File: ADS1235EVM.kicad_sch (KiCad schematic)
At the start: 60 parts, among them J1 Conn_01x04_Pin, J2 Conn_01x11_Pin, U1 ADS1235QWRHMRQ1, U2 LM27762, U5 UCC27524DGN

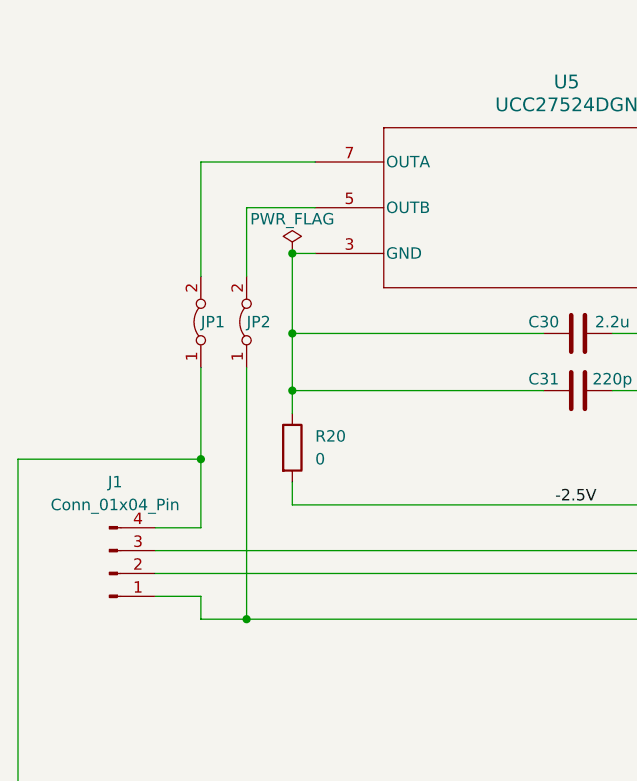
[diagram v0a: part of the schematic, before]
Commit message: Schematic - Jumpers removed + ERC OK
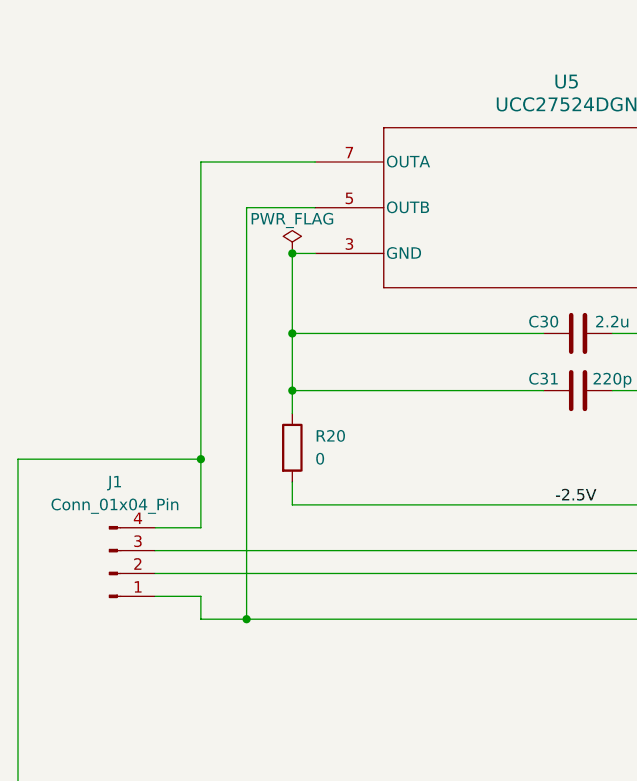
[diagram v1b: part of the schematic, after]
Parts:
- removed JP1, JP2: Jumper_2_Bridged, Jumper:SolderJumper-2_P1.3mm_Open_RoundedPad1.0x1.5mm, symbol Jumper:Jumper_2_Bridged
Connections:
- net at U5.5 (OUTB): now also J1.1 (Pin_1), R16.1
- net at U5.7 (OUTA): now also J1.4 (Pin_4), R17.1
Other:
- company: (none) -> LAAS - CNRS
- title: (none) -> Analog conditioning and filtering measurements
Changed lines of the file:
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@@
 (kicad_sch (version 20230121) (generator eeschema)
   (paper "A4")
+  (title_block
+    (title "Analog conditioning and filtering measurements")
+    (company "LAAS - CNRS")
+  )
   (junction (at 57.15 21.59) (diameter 0) (color 0 0 0 0)
   )
@@
     (stroke (width 0) (type default))
   )
-  (wire (pts (xy 41.91 114.3) (xy 41.91 142.24))
+  (wire (pts (xy 41.91 96.52) (xy 41.91 142.24))
     (stroke (width 0) (type default))
   )
@@
     (stroke (width 0) (type default))
   )
-  (wire (pts (xy 36.83 114.3) (xy 36.83 124.46))
+  (wire (pts (xy 36.83 91.44) (xy 36.83 124.46))
     (stroke (width 0) (type default))
   )
@@
     (stroke (width 0) (type default))
   )
-  (wire (pts (xy 41.91 96.52) (xy 41.91 104.14))
-    (stroke (width 0) (type default))
-  )
   (wire (pts (xy 109.22 59.69) (xy 109.22 63.5))
     (stroke (width 0) (type default))
@@
     (stroke (width 0) (type default))
   )
-  (wire (pts (xy 36.83 91.44) (xy 36.83 104.14))
-    (stroke (width 0) (type default))
-  )
   (wire (pts (xy 166.37 133.35) (xy 166.37 113.03))
     (stroke (width 0) (type default))
@@
     )
   )
-  (symbol (lib_id "Jumper:Jumper_2_Bridged") (at 41.91 109.22 90) (unit 1)
-    (in_bom yes) (on_board yes) (dnp no)
-    (property "Reference" "JP2" (at 41.91 109.22 90)
-      (effects (font (size 1.27 1.27)) (justify right))
-    )
-    (property "Value" "Jumper_2_Bridged" (at 22.86 107.95 90)
-      (effects (font (size 1.27 1.27)) (justify right) hide)
-    )
-    (property "Footprint" "Jumper:SolderJumper-2_P1.3mm_Open_RoundedPad1.0x1.5mm" (at 41.91 109.22 0)
-      (effects (font (size 1.27 1.27)) hide)
-    )
-    (property "Datasheet" "~" (at 41.91 109.22 0)
-      (effects (font (size 1.27 1.27)) hide)
-    )
-    (pin "1")
-    (pin "2")
-    (instances
-      (project "ADS1235EVM"
-        (path "/4faaba4a-da34-4767-a6c4-a9ccb9f4f95a"
-          (reference "JP2") (unit 1)
-        )
-      )
-      (project "PrincipleSchematicV4"
-        (path "/eda615d8-e9fe-47dd-8aa4-13a32693ef53"
-          (reference "JP2") (unit 1)
-        )
-      )
-    )
-  )
   (symbol (lib_id "Device:C") (at 236.22 134.62 0) (unit 1)
     (in_bom yes) (on_board yes) (dnp no)
@@
         )
       )
-    )
-  )
-  (symbol (lib_id "Jumper:Jumper_2_Bridged") (at 36.83 109.22 90) (unit 1)
-    (in_bom yes) (on_board yes) (dnp no)
-    (property "Reference" "JP1" (at 36.83 109.22 90)
-      (effects (font (size 1.27 1.27)) (justify right))
-    )
-    (property "Value" "Jumper_2_Bridged" (at 17.78 107.95 90)
-      (effects (font (size 1.27 1.27)) (justify right) hide)
-    )
-    (property "Footprint" "Jumper:SolderJumper-2_P1.3mm_Open_RoundedPad1.0x1.5mm" (at 36.83 109.22 0)
-      (effects (font (size 1.27 1.27)) hide)
-    )
-    (property "Datasheet" "~" (at 36.83 109.22 0)
-      (effects (font (size 1.27 1.27)) hide)
-    )
-    (pin "1")
-    (pin "2")
-    (instances
-      (project "ADS1235EVM"
-        (path "/4faaba4a-da34-4767-a6c4-a9ccb9f4f95a"
-          (reference "JP1") (unit 1)
-        )
-      )
-      (project "PrincipleSchematicV4"
-        (path "/eda615d8-e9fe-47dd-8aa4-13a32693ef53"
-          (reference "JP1") (unit 1)
-        )
-      )

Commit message: Schematic - Add of 2 jumpers to handle AC & DC excitation
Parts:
- added JP1: Jumper_2_Bridged, symbol Jumper:Jumper_2_Bridged
- added JP2: Jumper_2_Open, symbol Jumper:Jumper_2_Open
- added R22: 100k, Resistor_SMD:R_0402_1005Metric, symbol Device:R
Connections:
- net Avdd is gone; now on net -2.5V: C20.1, C22.1, C23.1, R21.1, R29.2, U1.4 (AVDD)
- net at R33.2, U5.2 (INA): now also JP1.1 (A), JP2.2 (B); no longer R35.2
- net at C30.2, C31.2, R21.2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: now also R22.2
- new net: JP2.1 (A), R35.2
- new net: JP1.2 (B), R22.1
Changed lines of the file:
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@@
   (junction (at 46.99 116.84) (diameter 0) (color 0 0 0 0)
   )
-  (junction (at 115.57 90.17) (diameter 0) (color 0 0 0 0)
-  )
   (junction (at 113.03 129.54) (diameter 0) (color 0 0 0 0)
   )
@@
   (junction (at 109.22 38.1) (diameter 0) (color 0 0 0 0)
   )
+  (junction (at 116.84 77.47) (diameter 0) (color 0 0 0 0)
+  )
   (junction (at 109.22 63.5) (diameter 0) (color 0 0 0 0)
   )
@@
   (junction (at 143.51 177.8) (diameter 0) (color 0 0 0 0)
   )
+  (junction (at 120.65 63.5) (diameter 0) (color 0 0 0 0)
+  )
   (junction (at 64.77 36.83) (diameter 0) (color 0 0 0 0)
   )
+  (junction (at 109.22 77.47) (diameter 0) (color 0 0 0 0)
+  )
   (junction (at 143.51 167.64) (diameter 0) (color 0 0 0 0)
   )
@@
     (stroke (width 0) (type default))
   )
-  (wire (pts (xy 109.22 63.5) (xy 170.18 63.5))
+  (wire (pts (xy 109.22 63.5) (xy 120.65 63.5))
     (stroke (width 0) (type default))
   )
@@
     (stroke (width 0) (type default))
   )
+  (wire (pts (xy 120.65 63.5) (xy 120.65 60.96))
+    (stroke (width 0) (type default))
+  )
   (wire (pts (xy 106.68 49.53) (xy 106.68 53.34))
     (stroke (width 0) (type default))
@@
     (stroke (width 0) (type default))
   )
+  (wire (pts (xy 116.84 115.57) (xy 116.84 119.38))
+    (stroke (width 0) (type default))
+  )
   (wire (pts (xy 148.59 187.96) (xy 148.59 186.69))
     (stroke (width 0) (type default))
@@
     (stroke (width 0) (type default))
   )
+  (wire (pts (xy 116.84 77.47) (xy 116.84 78.74))
+    (stroke (width 0) (type default))
+  )
   (wire (pts (xy 238.76 54.61) (xy 271.78 54.61))
     (stroke (width 0) (type default))
@@
     (stroke (width 0) (type default))
   )
-  (wire (pts (xy 120.65 67.31) (xy 120.65 60.96))
-    (stroke (width 0) (type default))
-  )
   (wire (pts (xy 240.03 116.84) (xy 240.03 119.38))
     (stroke (width 0) (type default))
@@
     (stroke (width 0) (type default))
   )
-  (wire (pts (xy 115.57 90.17) (xy 120.65 90.17))
-    (stroke (width 0) (type default))
-  )
   (wire (pts (xy 139.7 133.35) (xy 143.51 133.35))
     (stroke (width 0) (type default))
@@
     (stroke (width 0) (type default))
   )
-  (wire (pts (xy 106.68 49.53) (xy 109.22 49.53))
+  (wire (pts (xy 109.22 77.47) (xy 109.22 90.17))
     (stroke (width 0) (type default))
   )
-  (wire (pts (xy 109.22 90.17) (xy 115.57 90.17))
+  (wire (pts (xy 106.68 49.53) (xy 109.22 49.53))
     (stroke (width 0) (type default))
   )
@@
     (stroke (width 0) (type default))
   )
+  (wire (pts (xy 120.65 63.5) (xy 170.18 63.5))
+    (stroke (width 0) (type default))
+  )
   (wire (pts (xy 236.22 88.9) (xy 241.3 88.9))
     (stroke (width 0) (type default))
@@
     (stroke (width 0) (type default))
   )
+  (wire (pts (xy 116.84 77.47) (xy 120.65 77.47))
+    (stroke (width 0) (type default))
+  )
   (wire (pts (xy 143.51 167.64) (xy 148.59 167.64))
     (stroke (width 0) (type default))
@@
     (stroke (width 0) (type default))
   )
+  (wire (pts (xy 116.84 86.36) (xy 116.84 87.63))
+    (stroke (width 0) (type default))
+  )
   (wire (pts (xy 170.18 121.92) (xy 170.18 167.64))
     (stroke (width 0) (type default))
@@
     (stroke (width 0) (type default))
   )
+  (wire (pts (xy 120.65 67.31) (xy 120.65 63.5))
+    (stroke (width 0) (type default))
+  )
   (wire (pts (xy 119.38 49.53) (xy 119.38 50.8))
     (stroke (width 0) (type default))
@@
     (stroke (width 0) (type default))
   )
-  (wire (pts (xy 115.57 87.63) (xy 115.57 90.17))
+  (wire (pts (xy 109.22 76.2) (xy 109.22 77.47))
     (stroke (width 0) (type default))
   )
@@
     (stroke (width 0) (type default))
   )
+  (wire (pts (xy 109.22 77.47) (xy 116.84 77.47))
+    (stroke (width 0) (type default))
+  )
   (wire (pts (xy 236.22 91.44) (xy 241.3 91.44))
     (stroke (width 0) (type default))
@@
     (stroke (width 0) (type default))
   )
-  (wire (pts (xy 120.65 90.17) (xy 120.65 74.93))
+  (wire (pts (xy 120.65 77.47) (xy 120.65 74.93))
     (stroke (width 0) (type default))
   )
@@
     (stroke (width 0) (type default))
   )
-  (wire (pts (xy 116.84 97.79) (xy 116.84 119.38))
+  (wire (pts (xy 116.84 97.79) (xy 116.84 105.41))
     (stroke (width 0) (type default))
   )
@@
     )
   )
+  (symbol (lib_id "Jumper:Jumper_2_Open") (at 116.84 110.49 90) (unit 1)
+    (in_bom yes) (on_board yes) (dnp no) (fields_autoplaced)
+    (property "Reference" "JP2" (at 118.11 109.22 90)
+      (effects (font (size 1.27 1.27)) (justify right))
+    )
+    (property "Value" "Jumper_2_Open" (at 118.11 111.76 90)
+      (effects (font (size 1.27 1.27)) (justify right))
+    )
+    (property "Footprint" "" (at 116.84 110.49 0)
+      (effects (font (size 1.27 1.27)) hide)
+    )
+    (property "Datasheet" "~" (at 116.84 110.49 0)
+      (effects (font (size 1.27 1.27)) hide)
+    )
+    (pin "1")
+    (pin "2")
+    (instances
+      (project "ADS1235EVM"
+        (path "/4faaba4a-da34-4767-a6c4-a9ccb9f4f95a"
+          (reference "JP2") (unit 1)
+        )
+      )
+    )
+  )
   (symbol (lib_id "Device:R") (at 231.14 59.69 90) (unit 1)
     (in_bom yes) (on_board yes) (dnp no)
@@
   (symbol (lib_id "Device:R") (at 113.03 123.19 180) (unit 1)
     (in_bom yes) (on_board yes) (dnp no)
-    (property "Reference" "R36" (at 107.95 121.92 0)
-      (effects (font (size 1.27 1.27)) (justify right) hide)
+    (property "Reference" "R36" (at 110.49 124.46 90)
+      (effects (font (size 1.27 1.27)) (justify right))
     )
     (property "Value" "100k" (at 113.03 125.73 90)
@@
     )
   )
-  (symbol (lib_id "power:PWR_FLAG") (at 115.57 87.63 0) (unit 1)
+  (symbol (lib_id "power:PWR_FLAG") (at 109.22 76.2 0) (unit 1)
     (in_bom yes) (on_board yes) (dnp no)
-    (property "Reference" "#FLG04" (at 115.57 85.725 0)
+    (property "Reference" "#FLG04" (at 109.22 74.295 0)
       (effects (font (size 1.27 1.27)) hide)
     )
-    (property "Value" "PWR_FLAG" (at 115.57 83.82 0)
+    (property "Value" "PWR_FLAG" (at 109.22 72.39 0)
       (effects (font (size 1.27 1.27)))
     )
-    (property "Footprint" "" (at 115.57 87.63 0)
+    (property "Footprint" "" (at 109.22 76.2 0)
       (effects (font (size 1.27 1.27)) hide)
     )
-    (property "Datasheet" "~" (at 115.57 87.63 0)
+    (property "Datasheet" "~" (at 109.22 76.2 0)
       (effects (font (size 1.27 1.27)) hide)
     )
@@
     )
   )
+  (symbol (lib_id "Jumper:Jumper_2_Bridged") (at 116.84 92.71 90) (unit 1)
+    (in_bom yes) (on_board yes) (dnp no) (fields_autoplaced)
+    (property "Reference" "JP1" (at 118.11 91.44 90)
+      (effects (font (size 1.27 1.27)) (justify right))
+    )
+    (property "Value" "Jumper_2_Bridged" (at 118.11 93.98 90)
+      (effects (font (size 1.27 1.27)) (justify right))
+    )
+    (property "Footprint" "" (at 116.84 92.71 0)
+      (effects (font (size 1.27 1.27)) hide)
+    )
+    (property "Datasheet" "~" (at 116.84 92.71 0)
+      (effects (font (size 1.27 1.27)) hide)
+    )
+    (pin "1")
+    (pin "2")
+    (instances
+      (project "ADS1235EVM"
+        (path "/4faaba4a-da34-4767-a6c4-a9ccb9f4f95a"
+          (reference "JP1") (unit 1)
+        )
+      )
+    )
+  )
   (symbol (lib_id "power:GND") (at 81.28 63.5 0) (unit 1)
     (in_bom yes) (on_board yes) (dnp no)
@@
     )
   )
+  (symbol (lib_id "Device:R") (at 116.84 82.55 180) (unit 1)
+    (in_bom yes) (on_board yes) (dnp no)
+    (property "Reference" "R22" (at 119.38 83.82 90)
+      (effects (font (size 1.27 1.27)) (justify right))
+    )
+    (property "Value" "100k" (at 116.84 85.09 90)
+      (effects (font (size 1.27 1.27)) (justify right))
+    )
+    (property "Footprint" "Resistor_SMD:R_0402_1005Metric" (at 118.618 82.55 90)
+      (effects (font (size 1.27 1.27)) hide)
+    )
+    (property "Datasheet" "~" (at 116.84 82.55 0)
+      (effects (font (size 1.27 1.27)) hide)
+    )
+    (pin "1")
+    (pin "2")
+    (instances
+      (project "ADS1235EVM"
+        (path "/4faaba4a-da34-4767-a6c4-a9ccb9f4f95a"
+          (reference "R22") (unit 1)
+        )
+      )
+      (project "PrincipleSchematicV4"
+        (path "/eda615d8-e9fe-47dd-8aa4-13a32693ef53"
+          (reference "R35") (unit 1)
+        )
+      )
+    )
+  )
   (symbol (lib_id "Device:C") (at 148.59 128.27 0) (unit 1)
     (in_bom yes) (on_board yes) (dnp no) (fields_autoplaced)
@@
   (symbol (lib_id "Device:R") (at 116.84 123.19 180) (unit 1)
     (in_bom yes) (on_board yes) (dnp no)
-    (property "Reference" "R35" (at 111.76 121.92 0)
-      (effects (font (size 1.27 1.27)) (justify right) hide)
+    (property "Reference" "R35" (at 119.38 124.46 90)
+      (effects (font (size 1.27 1.27)) (justify right))
     )
     (property "Value" "100k" (at 116.84 125.73 90)

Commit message: Association Schematic & PCB
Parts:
- removed JP1: Jumper_2_Bridged, symbol Jumper:Jumper_2_Bridged
- removed JP2: Jumper_2_Open, symbol Jumper:Jumper_2_Open
- added JP1: Jumper_3_Bridged12, Jumper:SolderJumper-3_P1.3mm_Bridged12_RoundedPad1.0x1.5mm, symbol Jumper:Jumper_3_Bridged12
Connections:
- net nACX2 is gone; now on net Avdd: U1.29 (AIN1)
- net -2.5V: no longer C20.1, C22.1, C23.1, R21.1, R29.2, U1.4 (AVDD)
- net at R33.2, U5.2 (INA): now also JP1.2 (C)
- net at C12.2, C14.1, R19.2: now also U1.26 (AIN4); no longer U1.25 (AIN5)
- net at R35.2: now also JP1.3 (B)
- net at C12.1, C13.2, R18.2: now also U1.25 (AIN5); no longer U1.26 (AIN4)
- net at R22.1: now also JP1.1 (A)
- net nACX1 renamed Avdd
- net Avdd: now also C20.1, C22.1, C23.1, R21.1, R29.2, U1.4 (AVDD)
- no-connect marks 12 -> 10
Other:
- moved on the sheet: C14
